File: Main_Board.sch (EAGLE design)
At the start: 40 parts, among them U1 RN4020RN4020

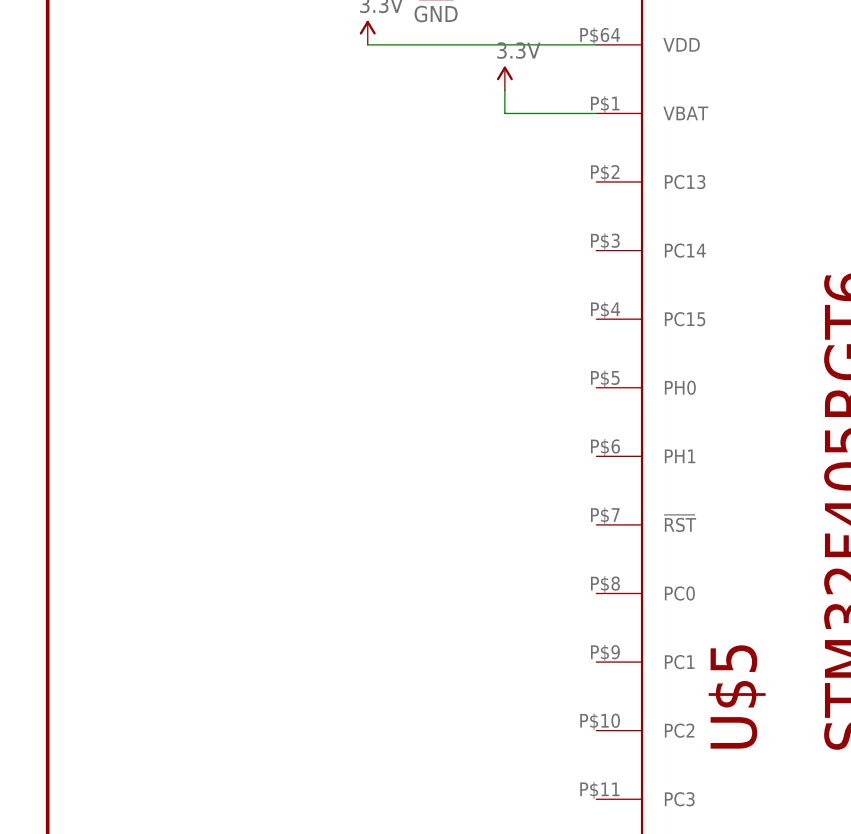
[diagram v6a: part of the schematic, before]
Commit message: Added oscilator to schematic
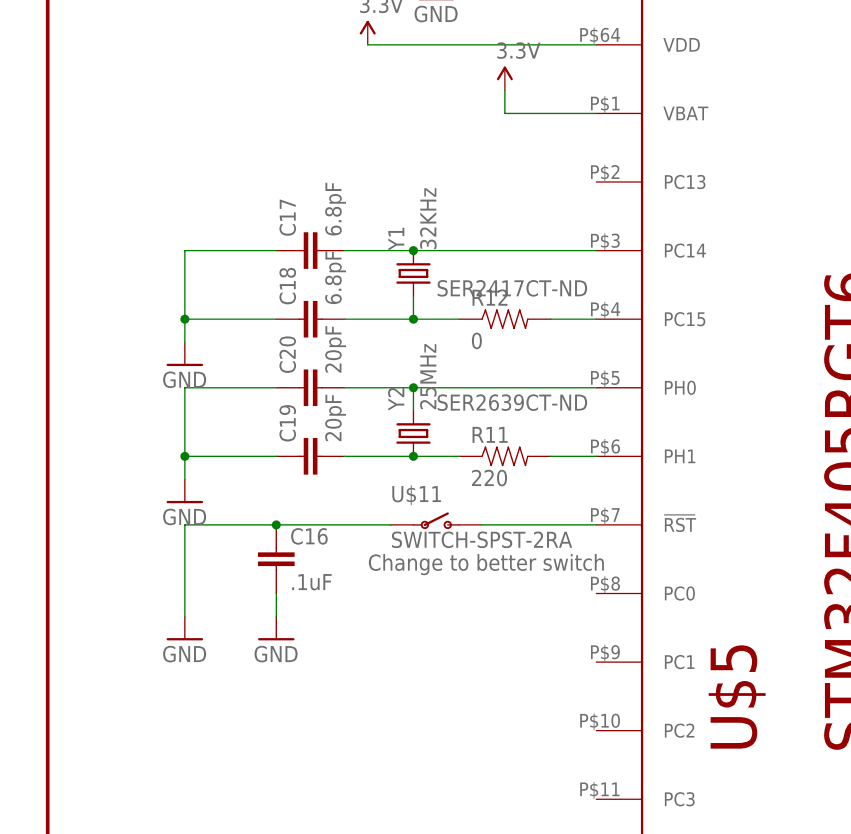
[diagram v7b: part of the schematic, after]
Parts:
- added C16: .1uF, SparkFun-Passives:CAP0805
- added C17, C18: 6.8pF, SparkFun-Passives:CAP0805
- added C19, C20: 20pF, SparkFun-Passives:CAP0805
- added R11: 220, SparkFun-Passives:RESISTOR0805-RES
- added R12: 0, SparkFun-Passives:RESISTOR0805-RES
- added U$11: SWITCH-SPST-2RA, SparkFun-Electromechanical:SWITCH-SPST-2RA
- added Y1: 32KHz, SparkFun-FreqCtrl:CRYSTALCRYSTAL-SMD-5X3-12MHZ
- added Y2: 25MHz, SparkFun-FreqCtrl:CRYSTALCRYSTAL-SMD-5X3-12MHZ
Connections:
- new net N$12: C17.2, U$5.PC14, Y1.2
- new net N$17: C19.2, R11.1, Y2.1
- new net N$18: C18.2, R12.1, Y1.1
- new net N$19: R11.2, U$5.PH1
- new net N$20: C20.2, U$5.PH0, Y2.2
- new net N$21: R12.2, U$5.PC15
- new net N$7: U$11.O, U$5.!RST
- net GND: now also C16.1, C16.2, C17.1, C18.1, C19.1, C20.1, U$11.P
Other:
- note added: "Change to better switch"
- note added: "SER2417CT-ND"
- note added: "SER2639CT-ND"
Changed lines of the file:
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@@
 <part name="GND30" library="SparkFun-Aesthetics" deviceset="GND" device=""/>
 <part name="GND31" library="SparkFun-Aesthetics" deviceset="GND" device=""/>
+<part name="U$11" library="SparkFun-Electromechanical" deviceset="SWITCH-SPST-2" device="RA"/>
+<part name="C16" library="SparkFun-Passives" deviceset="CAP" device="0805" value=".1uF"/>
+<part name="GND32" library="SparkFun-Aesthetics" deviceset="GND" device=""/>
+<part name="GND33" library="SparkFun-Aesthetics" deviceset="GND" device=""/>
+<part name="Y1" library="SparkFun-FreqCtrl" deviceset="CRYSTAL" device="CRYSTAL-SMD-5X3-12MHZ" value="32KHz"/>
+<part name="C17" library="SparkFun-Passives" deviceset="CAP" device="0805" value="6.8pF"/>
+<part name="C18" library="SparkFun-Passives" deviceset="CAP" device="0805" value="6.8pF"/>
+<part name="GND34" library="SparkFun-Aesthetics" deviceset="GND" device=""/>
+<part name="Y2" library="SparkFun-FreqCtrl" deviceset="CRYSTAL" device="CRYSTAL-SMD-5X3-12MHZ" value="25MHz"/>
+<part name="C19" library="SparkFun-Passives" deviceset="CAP" device="0805" value="20pF"/>
+<part name="C20" library="SparkFun-Passives" deviceset="CAP" device="0805" value="20pF"/>
+<part name="GND35" library="SparkFun-Aesthetics" deviceset="GND" device=""/>
+<part name="R11" library="SparkFun-Passives" deviceset="RESISTOR" device="0805-RES" value="220"/>
+<part name="R12" library="SparkFun-Passives" deviceset="RESISTOR" device="0805-RES" value="0"/>
 </parts>
 <sheets>
@@
 MC1_INH_3.3
 MC2_INH_3.3</text>
+<text x="309.88" y="91.44" size="1.778" layer="95">Change to better switch</text>
+<text x="317.5" y="121.92" size="1.778" layer="95">SER2417CT-ND</text>
+<text x="317.5" y="109.22" size="1.778" layer="95">SER2639CT-ND</text>
 </plain>
 <instances>
@@
 <instance part="GND30" gate="1" x="538.48" y="-157.48"/>
 <instance part="GND31" gate="1" x="566.42" y="-165.1"/>
+<instance part="U$11" gate="G$1" x="317.5" y="96.52"/>
+<instance part="C16" gate="G$1" x="299.72" y="91.44"/>
+<instance part="GND32" gate="1" x="299.72" y="83.82"/>
+<instance part="GND33" gate="1" x="289.56" y="83.82"/>
+<instance part="Y1" gate="G$1" x="314.96" y="124.46" rot="R90"/>
+<instance part="C17" gate="G$1" x="304.8" y="127" rot="R90"/>
+<instance part="C18" gate="G$1" x="304.8" y="119.38" rot="R90"/>
+<instance part="GND34" gate="1" x="289.56" y="114.3"/>
+<instance part="Y2" gate="G$1" x="314.96" y="106.68" rot="R90"/>
+<instance part="C19" gate="G$1" x="304.8" y="104.14" rot="R90"/>
+<instance part="C20" gate="G$1" x="304.8" y="111.76" rot="R90"/>
+<instance part="GND35" gate="1" x="289.56" y="99.06"/>
+<instance part="R11" gate="G$1" x="325.12" y="104.14"/>
+<instance part="R12" gate="G$1" x="325.12" y="119.38"/>
 </instances>
 <busses>
@@
 <wire x1="477.52" y1="-154.94" x2="467.36" y2="-154.94" width="0.1524" layer="91"/>
 </segment>
+<segment>
+<pinref part="C16" gate="G$1" pin="2"/>
+<pinref part="GND32" gate="1" pin="GND"/>
+<wire x1="299.72" y1="86.36" x2="299.72" y2="88.9" width="0.1524" layer="91"/>
+</segment>
+<segment>
+<pinref part="GND33" gate="1" pin="GND"/>
+<wire x1="289.56" y1="86.36" x2="289.56" y2="96.52" width="0.1524" layer="91"/>
+<pinref part="U$11" gate="G$1" pin="P"/>
+<pinref part="C16" gate="G$1" pin="1"/>
+<wire x1="312.42" y1="96.52" x2="299.72" y2="96.52" width="0.1524" layer="91"/>
+<wire x1="289.56" y1="96.52" x2="299.72" y2="96.52" width="0.1524" layer="91"/>
+<junction x="299.72" y="96.52"/>
+</segment>
+<segment>
+<pinref part="C17" gate="G$1" pin="1"/>
+<pinref part="GND34" gate="1" pin="GND"/>
+<wire x1="299.72" y1="127" x2="289.56" y2="127" width="0.1524" layer="91"/>
+<wire x1="289.56" y1="127" x2="289.56" y2="119.38" width="0.1524" layer="91"/>
+<pinref part="C18" gate="G$1" pin="1"/>
+<wire x1="289.56" y1="119.38" x2="289.56" y2="116.84" width="0.1524" layer="91"/>
+<wire x1="299.72" y1="119.38" x2="289.56" y2="119.38" width="0.1524" layer="91"/>
+<junction x="289.56" y="119.38"/>
+</segment>
+<segment>
+<pinref part="C20" gate="G$1" pin="1"/>
+<pinref part="GND35" gate="1" pin="GND"/>
+<wire x1="299.72" y1="111.76" x2="289.56" y2="111.76" width="0.1524" layer="91"/>
+<wire x1="289.56" y1="111.76" x2="289.56" y2="104.14" width="0.1524" layer="91"/>
+<pinref part="C19" gate="G$1" pin="1"/>
+<wire x1="289.56" y1="104.14" x2="289.56" y2="101.6" width="0.1524" layer="91"/>
+<wire x1="299.72" y1="104.14" x2="289.56" y2="104.14" width="0.1524" layer="91"/>
+<junction x="289.56" y="104.14"/>
+</segment>
 </net>
 <net name="N$1" class="0">
@@
 </segment>
 </net>
+<net name="N$7" class="0">
+<segment>
+<pinref part="U$5" gate="G$1" pin="!RST"/>
+<pinref part="U$11" gate="G$1" pin="O"/>
+<wire x1="335.28" y1="96.52" x2="322.58" y2="96.52" width="0.1524" layer="91"/>
+</segment>
+</net>
+<net name="N$12" class="0">
+<segment>
+<pinref part="Y1" gate="G$1" pin="2"/>
+<pinref part="U$5" gate="G$1" pin="PC14"/>
+<wire x1="314.96" y1="127" x2="335.28" y2="127" width="0.1524" layer="91"/>
+<pinref part="C17" gate="G$1" pin="2"/>
+<wire x1="307.34" y1="127" x2="314.96" y2="127" width="0.1524" layer="91"/>
+<junction x="314.96" y="127"/>
+</segment>
+</net>
+<net name="N$18" class="0">
+<segment>
+<pinref part="Y1" gate="G$1" pin="1"/>
+<wire x1="314.96" y1="119.38" x2="314.96" y2="121.92" width="0.1524" layer="91"/>
+<pinref part="C18" gate="G$1" pin="2"/>
+<wire x1="307.34" y1="119.38" x2="314.96" y2="119.38" width="0.1524" layer="91"/>
+<pinref part="R12" gate="G$1" pin="1"/>
+<wire x1="320.04" y1="119.38" x2="314.96" y2="119.38" width="0.1524" layer="91"/>
+<junction x="314.96" y="119.38"/>
+</segment>
+</net>
+<net name="N$17" class="0">
+<segment>
+<pinref part="C19" gate="G$1" pin="2"/>
+<pinref part="Y2" gate="G$1" pin="1"/>
+<wire x1="307.34" y1="104.14" x2="314.96" y2="104.14" width="0.1524" layer="91"/>
+<pinref part="R11" gate="G$1" pin="1"/>
+<wire x1="314.96" y1="104.14" x2="320.04" y2="104.14" width="0.1524" layer="91"/>
+<junction x="314.96" y="104.14"/>
+</segment>
+</net>
+<net name="N$19" class="0">
+<segment>
+<pinref part="R11" gate="G$1" pin="2"/>
+<pinref part="U$5" gate="G$1" pin="PH1"/>
+<wire x1="330.2" y1="104.14" x2="335.28" y2="104.14" width="0.1524" layer="91"/>
+</segment>
+</net>
+<net name="N$20" class="0">
+<segment>
+<pinref part="C20" gate="G$1" pin="2"/>
+<pinref part="U$5" gate="G$1" pin="PH0"/>
+<wire x1="307.34" y1="111.76" x2="314.96" y2="111.76" width="0.1524" layer="91"/>
+<pinref part="Y2" gate="G$1" pin="2"/>
+<wire x1="314.96" y1="111.76" x2="335.28" y2="111.76" width="0.1524" layer="91"/>
+<wire x1="314.96" y1="109.22" x2="314.96" y2="111.76" width="0.1524" layer="91"/>
+<junction x="314.96" y="111.76"/>
+</segment>
+</net>
+<net name="N$21" class="0">
+<segment>
+<pinref part="R12" gate="G$1" pin="2"/>
+<pinref part="U$5" gate="G$1" pin="PC15"/>
+<wire x1="330.2" y1="119.38" x2="335.28" y2="119.38" width="0.1524" layer="91"/>
+</segment>
+</net>

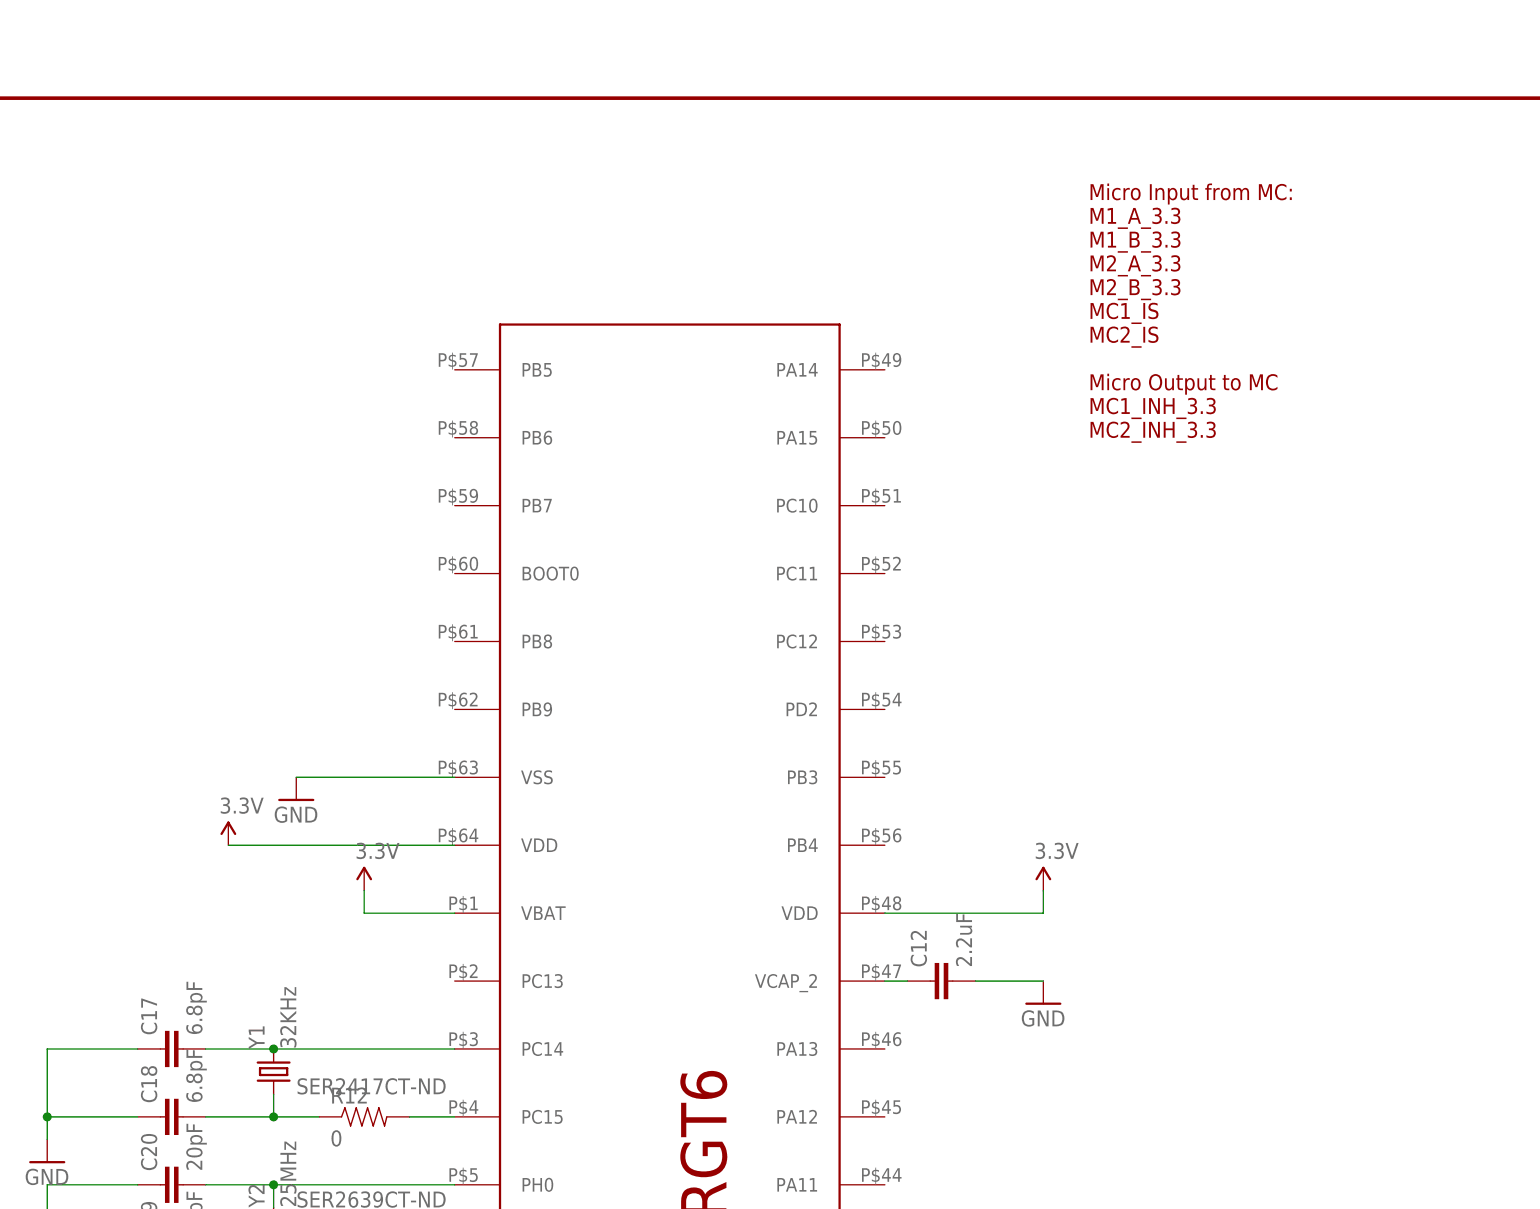
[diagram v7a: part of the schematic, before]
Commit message: Added most remaining STM requirements
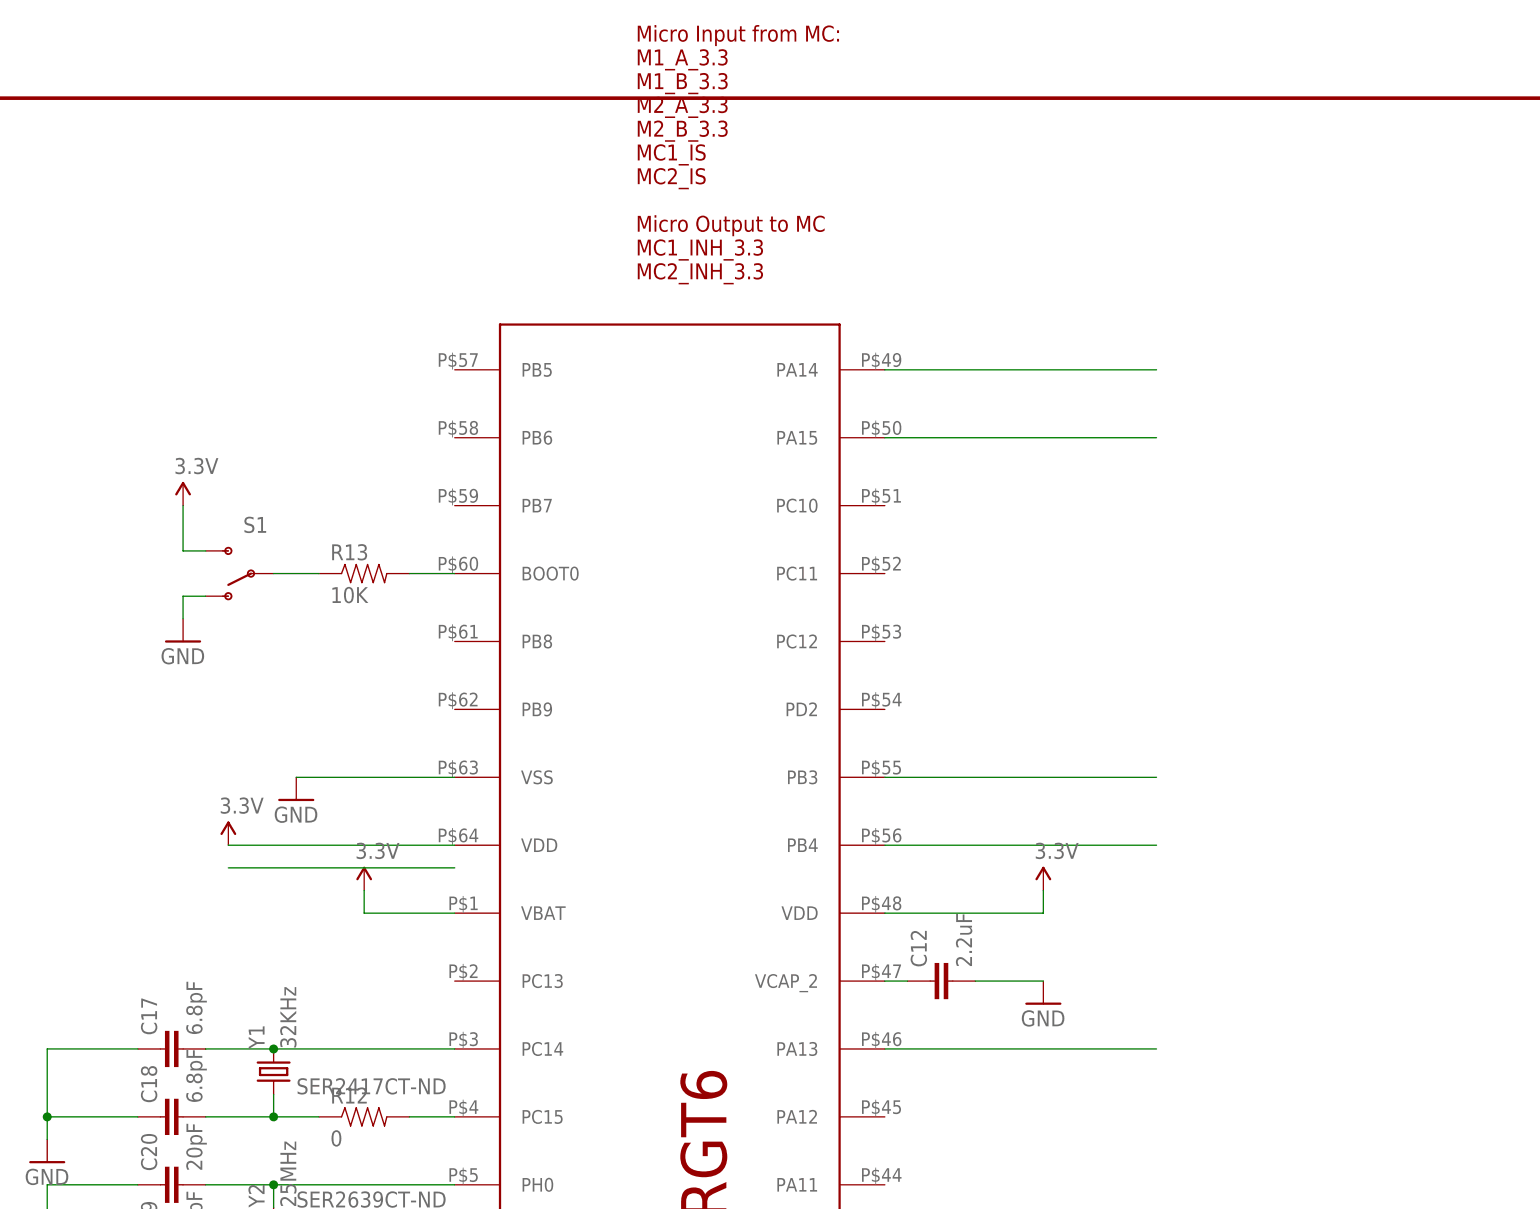
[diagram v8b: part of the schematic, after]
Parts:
- added R13: 10K, SparkFun-Passives:RESISTOR0805-RES
- added S1: (no value), SparkFun-Electromechanical:SWITCH-SPDTPTH_LOCK
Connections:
- new net N$22: R13.2, U$5.BOOT0
- new net N$23: R13.1, S1.P
- new net N$24: U$5.PA13
- new net N$25: U$5.PA14
- new net N$26: U$5.PA15
- new net N$27: U$5.PB3
- new net N$28: U$5.PB4
- net 3.3V: now also S1.S
- net GND: now also S1.O
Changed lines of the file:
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@@
 <part name="R11" library="SparkFun-Passives" deviceset="RESISTOR" device="0805-RES" value="220"/>
 <part name="R12" library="SparkFun-Passives" deviceset="RESISTOR" device="0805-RES" value="0"/>
+<part name="S1" library="SparkFun-Electromechanical" deviceset="SWITCH-SPDT" device="PTH_LOCK"/>
+<part name="R13" library="SparkFun-Passives" deviceset="RESISTOR" device="0805-RES" value="10K"/>
+<part name="SUPPLY19" library="SparkFun-Aesthetics" deviceset="3.3V" device=""/>
+<part name="GND36" library="SparkFun-Aesthetics" deviceset="GND" device=""/>
 </parts>
 <sheets>
@@
 <text x="7.62" y="-66.04" size="6.4516" layer="95">Power Conversion</text>
 <text x="472.44" y="-71.12" size="6.4516" layer="95">Bluetooth</text>
-<text x="406.4" y="195.58" size="1.778" layer="94">Micro Input from MC:
+<text x="355.6" y="213.36" size="1.778" layer="94">Micro Input from MC:
 M1_A_3.3
 M1_B_3.3
@@
 <instance part="R11" gate="G$1" x="325.12" y="104.14"/>
 <instance part="R12" gate="G$1" x="325.12" y="119.38"/>
+<instance part="S1" gate="1" x="312.42" y="180.34" rot="R180"/>
+<instance part="R13" gate="G$1" x="325.12" y="180.34"/>
+<instance part="SUPPLY19" gate="G$1" x="304.8" y="187.96"/>
+<instance part="GND36" gate="1" x="304.8" y="172.72"/>
 </instances>
 <busses>
@@
 <junction x="289.56" y="104.14"/>
 </segment>
+<segment>
+<pinref part="S1" gate="1" pin="O"/>
+<pinref part="GND36" gate="1" pin="GND"/>
+<wire x1="307.34" y1="177.8" x2="304.8" y2="177.8" width="0.1524" layer="91"/>
+<wire x1="304.8" y1="177.8" x2="304.8" y2="175.26" width="0.1524" layer="91"/>
+</segment>
 </net>
 <net name="N$1" class="0">
@@
 <junction x="546.1" y="-149.86"/>
 </segment>
+<segment>
+<wire x1="335.28" y1="147.32" x2="309.88" y2="147.32" width="0.1524" layer="91"/>
+</segment>
+<segment>
+<pinref part="S1" gate="1" pin="S"/>
+<pinref part="SUPPLY19" gate="G$1" pin="3.3V"/>
+<wire x1="307.34" y1="182.88" x2="304.8" y2="182.88" width="0.1524" layer="91"/>
+<wire x1="304.8" y1="182.88" x2="304.8" y2="187.96" width="0.1524" layer="91"/>
+</segment>
 </net>
 <net name="N$15" class="0">
@@
 </segment>
 </net>
+<net name="N$22" class="0">
+<segment>
+<pinref part="R13" gate="G$1" pin="2"/>
+<pinref part="U$5" gate="G$1" pin="BOOT0"/>
+<wire x1="330.2" y1="180.34" x2="335.28" y2="180.34" width="0.1524" layer="91"/>
+</segment>
+</net>
+<net name="N$23" class="0">
+<segment>
+<pinref part="R13" gate="G$1" pin="1"/>
+<pinref part="S1" gate="1" pin="P"/>
+<wire x1="320.04" y1="180.34" x2="314.96" y2="180.34" width="0.1524" layer="91"/>
+</segment>
+</net>
+<net name="N$24" class="0">
+<segment>
+<pinref part="U$5" gate="G$1" pin="PA13"/>
+<wire x1="383.54" y1="127" x2="414.02" y2="127" width="0.1524" layer="91"/>
+</segment>
+</net>
+<net name="N$25" class="0">
+<segment>
+<pinref part="U$5" gate="G$1" pin="PA14"/>
+<wire x1="383.54" y1="203.2" x2="414.02" y2="203.2" width="0.1524" layer="91"/>
+</segment>
+</net>
+<net name="N$26" class="0">
+<segment>
+<pinref part="U$5" gate="G$1" pin="PA15"/>
+<wire x1="383.54" y1="195.58" x2="414.02" y2="195.58" width="0.1524" layer="91"/>
+</segment>
+</net>
+<net name="N$27" class="0">
+<segment>
+<pinref part="U$5" gate="G$1" pin="PB3"/>
+<wire x1="383.54" y1="157.48" x2="414.02" y2="157.48" width="0.1524" layer="91"/>
+</segment>
+</net>
+<net name="N$28" class="0">
+<segment>
+<wire x1="383.54" y1="149.86" x2="414.02" y2="149.86" width="0.1524" layer="91"/>
+<pinref part="U$5" gate="G$1" pin="PB4"/>
+</segment>
+</net>
